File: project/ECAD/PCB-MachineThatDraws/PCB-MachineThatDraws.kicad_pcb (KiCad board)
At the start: 2 copper layers, 53.5 x 83 mm, 29 parts, among them J1 SD_Card_Device, J10 Conn_02x03_Odd_Even, J11 Conn_02x03_Odd_Even, J2 SDA/SCL/VCC/GND, J3 Switch, J4 Limit_Switch_X, J5 Moteur, J6 Moteur, J7 Barrel_Jack_Switch, J8 Screw_Terminal_01x02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

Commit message: pcb up
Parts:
- J3, J4: footprint Connector_JST:JST_PH_B3B-PH-K_1x03_P2.00mm_Vertical -> Connector_PinHeader_2.54mm:PinHeader_1x03_P2.54mm_Vertical
- turned J3 to 90 degrees
- turned J4 to 90 degrees
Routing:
- net GND: track 223.5 -> 0.00 mm
- net D9: track 30.2 -> 31.4 mm
- net D8: track 15.1 -> 16.3 mm
- net +3.3V: track 129.6 -> 129.1 mm
- added copper zone on F.Cu, net GND

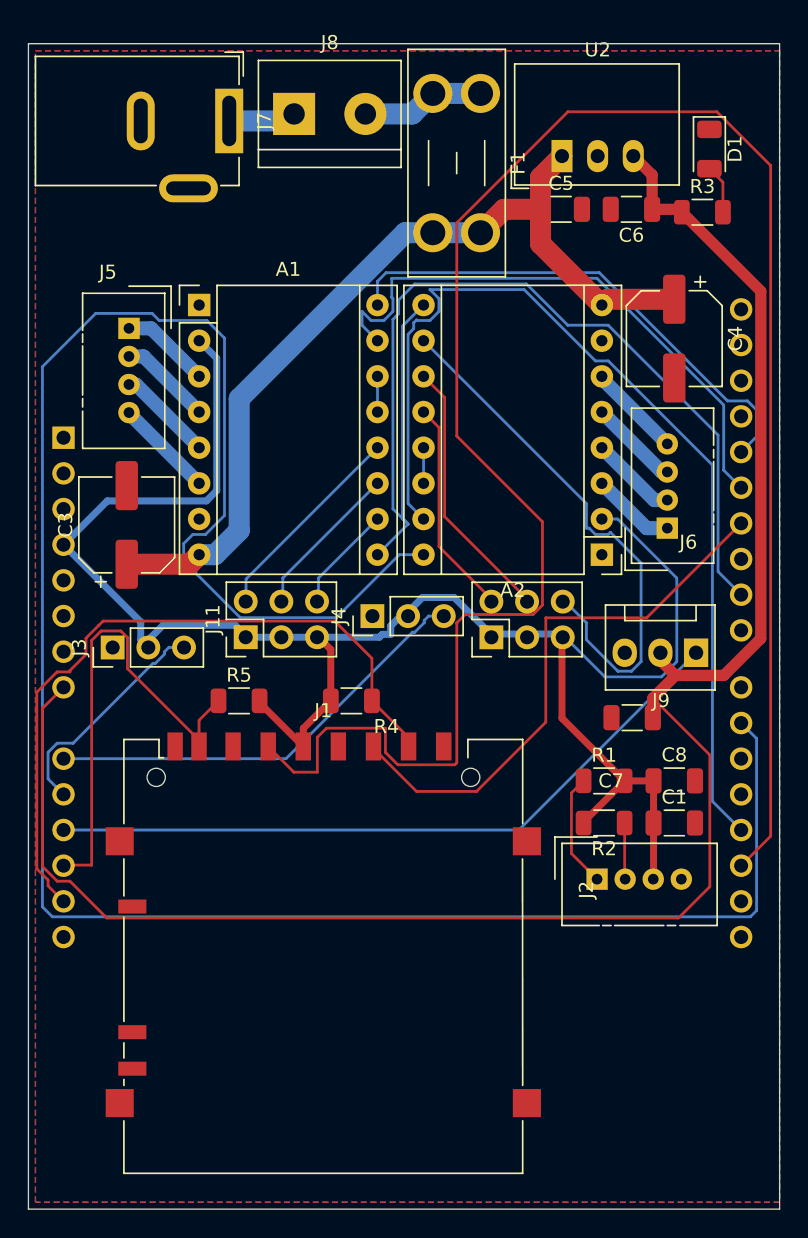
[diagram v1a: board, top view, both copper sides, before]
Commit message: pcb + sch up
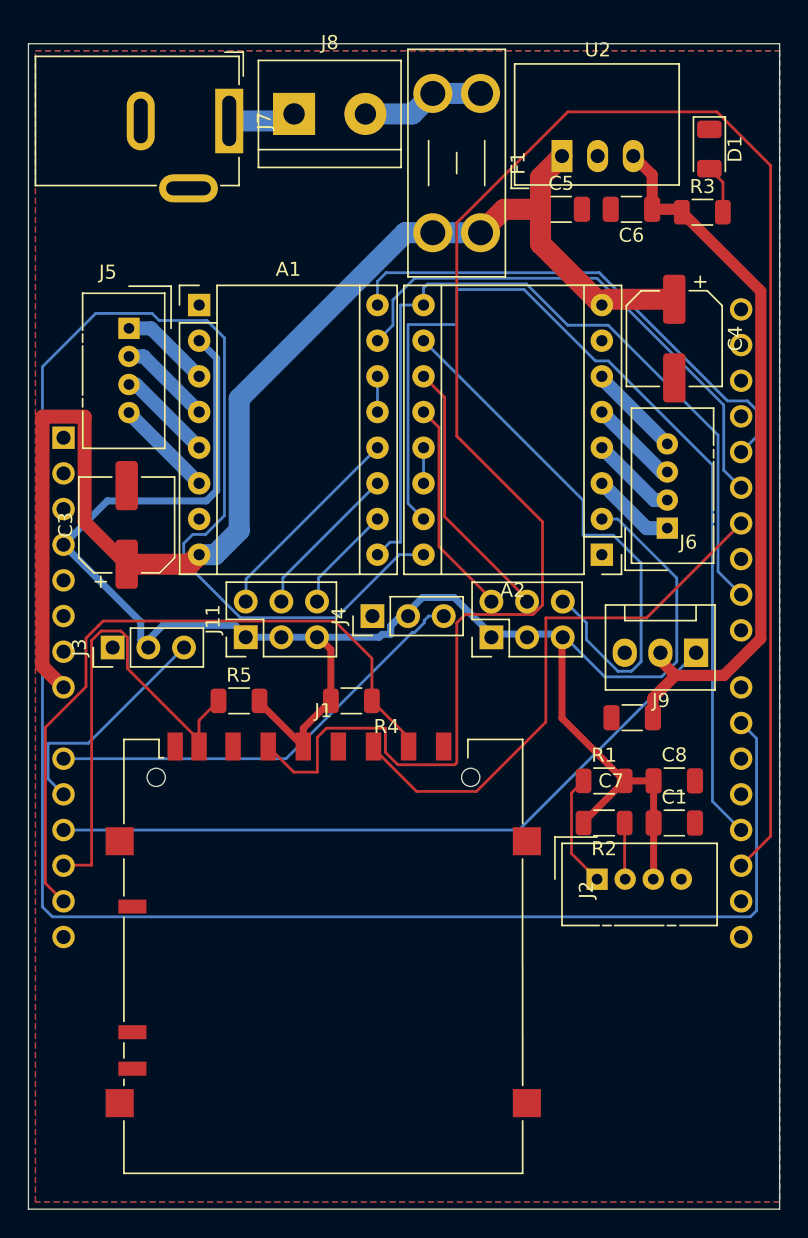
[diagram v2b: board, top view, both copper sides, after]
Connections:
- U1 pad 8: +5V -> +12V
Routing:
- net +5V: track 130.6 -> 52.1 mm
- net +12V: track 63.8 -> 98.5 mm
- net Enable: track 75.8 -> 59.4 mm
- net D13: track 41.5 -> 37.7 mm
- net D05: track 50.8 -> 49.8 mm

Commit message: pcb opti
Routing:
- net D14: track 157.1 -> 34.2 mm
- net D18: track 143.4 -> 38.9 mm
- net +12V: track 98.5 -> 73.8 mm
- net D19: track 34.7 -> 18.5 mm
- net Net-(A2-MS1): track 39.3 -> 23.3 mm
- net D10: track 70.5 -> 56.1 mm
- net +3.3V: track 129.1 -> 115.4 mm
- net D11: track 39.8 -> 51.5 mm
- net +5V: track 52.1 -> 44.1 mm
- net D13: track 37.7 -> 32.4 mm
- net D05: track 49.8 -> 47.3 mm
- net Net-(A2-MS3): track 15.2 -> 17.6 mm
- net D12: track 36.4 -> 34.5 mm
- net Net-(A2-MS2): track 18.8 -> 20.4 mm

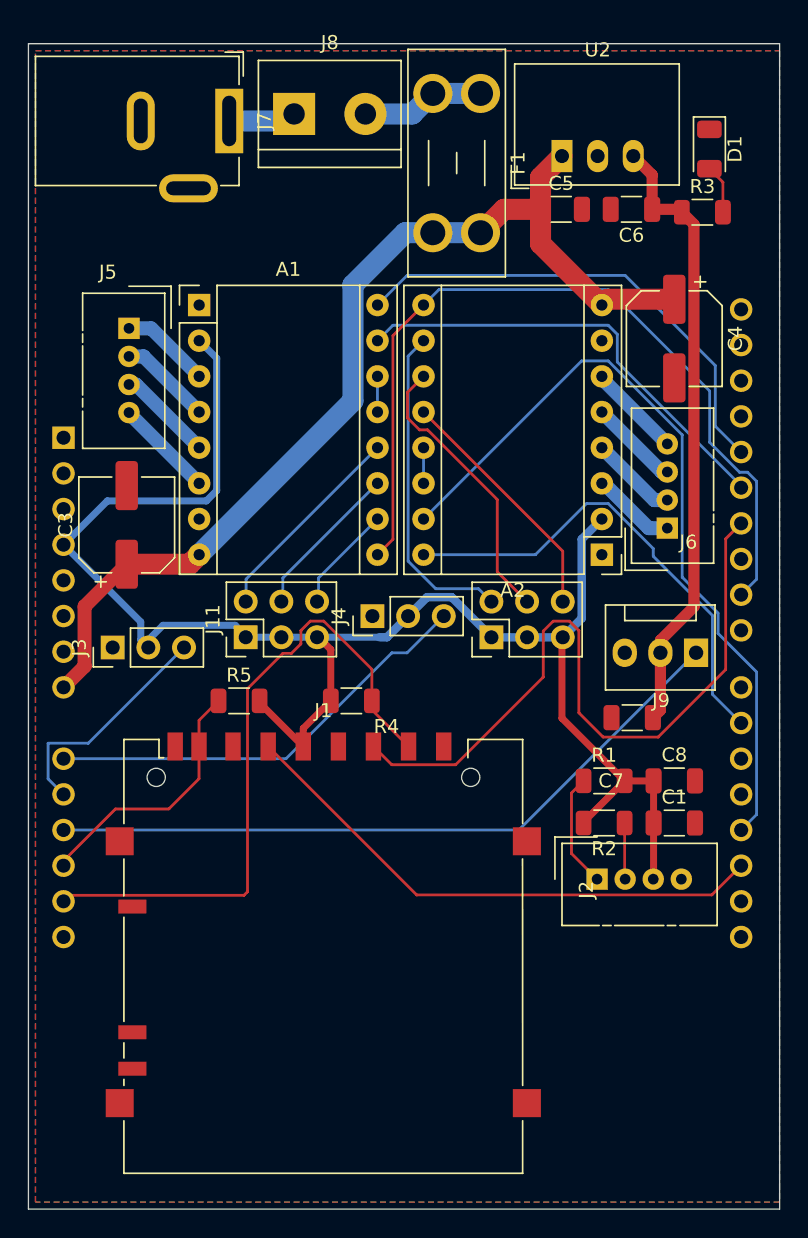
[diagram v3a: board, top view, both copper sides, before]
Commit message: pcb up, 0 erreurs au drc
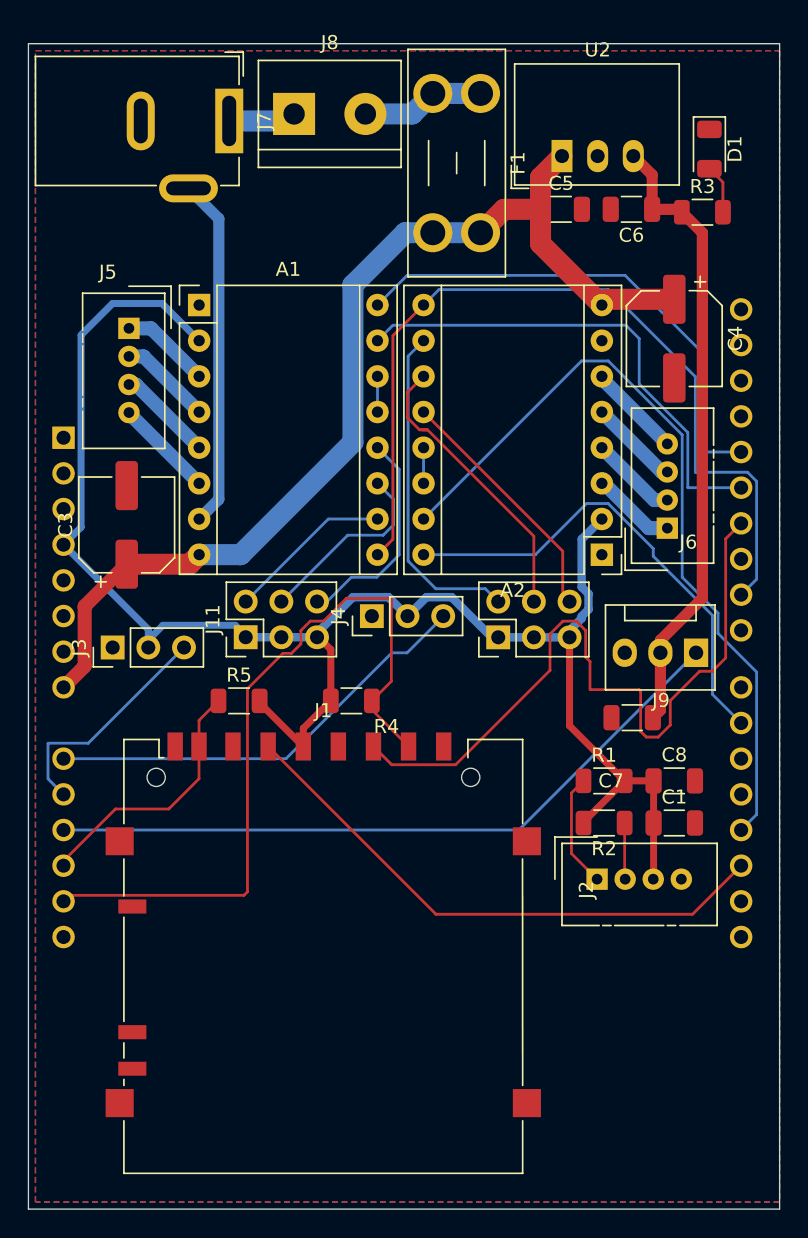
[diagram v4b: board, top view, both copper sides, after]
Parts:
- moved J10 0.49 mm to (130.0, 76.8)
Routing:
- net GND: track 0.00 -> 25.1 mm
- net D05: track 47.3 -> 53.5 mm
- net Net-(A1-MS1): track 7.62 -> 11.8 mm
- net +3.3V: track 115.4 -> 118.9 mm
- net D13: track 32.4 -> 35.3 mm
- net Net-(A1-MS2): track 11.3 -> 13.7 mm
- net Enable: track 59.6 -> 61.5 mm
- net +12V: track 73.8 -> 75.5 mm
- net D12: track 34.5 -> 36.1 mm
- net D18: track 38.9 -> 40.1 mm
- net D11: track 51.5 -> 52.2 mm
- net Net-(A2-MS2): track 20.4 -> 21.0 mm
- net Net-(A1-MS3): track 14.9 -> 15.5 mm

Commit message: pcb correction
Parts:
- J5, J6: footprint Connector:NS-Tech_Grove_1x04_P2mm_Vertical -> Connector_PinHeader_2.54mm:PinHeader_1x04_P2.54mm_Vertical
- J9: footprint Connector:FanPinHeader_1x03_P2.54mm_Vertical -> Connector_PinHeader_2.54mm:PinHeader_1x03_P2.54mm_Vertical
- moved J6 1.47 mm to (141.0, 70.1)
- moved J5 0.58 mm to (103.7, 54.2)
- turned J9 to -90 degrees
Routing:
- net +3.3V: track 118.9 -> 113.5 mm
- net D14: track 34.2 -> 36.3 mm
- net D10: track 56.1 -> 57.7 mm
- net Net-(A2-2B): track 6.74 -> 5.79 mm
- net Net-(A2-2A): track 6.43 -> 5.79 mm
